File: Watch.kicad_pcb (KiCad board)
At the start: 2 copper layers, 34.5 x 38.6 mm, 42 parts, among them J1 USB_C_Receptacle_USB2.0_14P, Q1 2N3904, Q2 2N3904, Q3 2N3904, Q4 2N3904, SW1 SW_Push, SW3 SW_Push, SW4 SW_Push, U1 MCP73831-2-OT, U3 AP2112K-3.3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

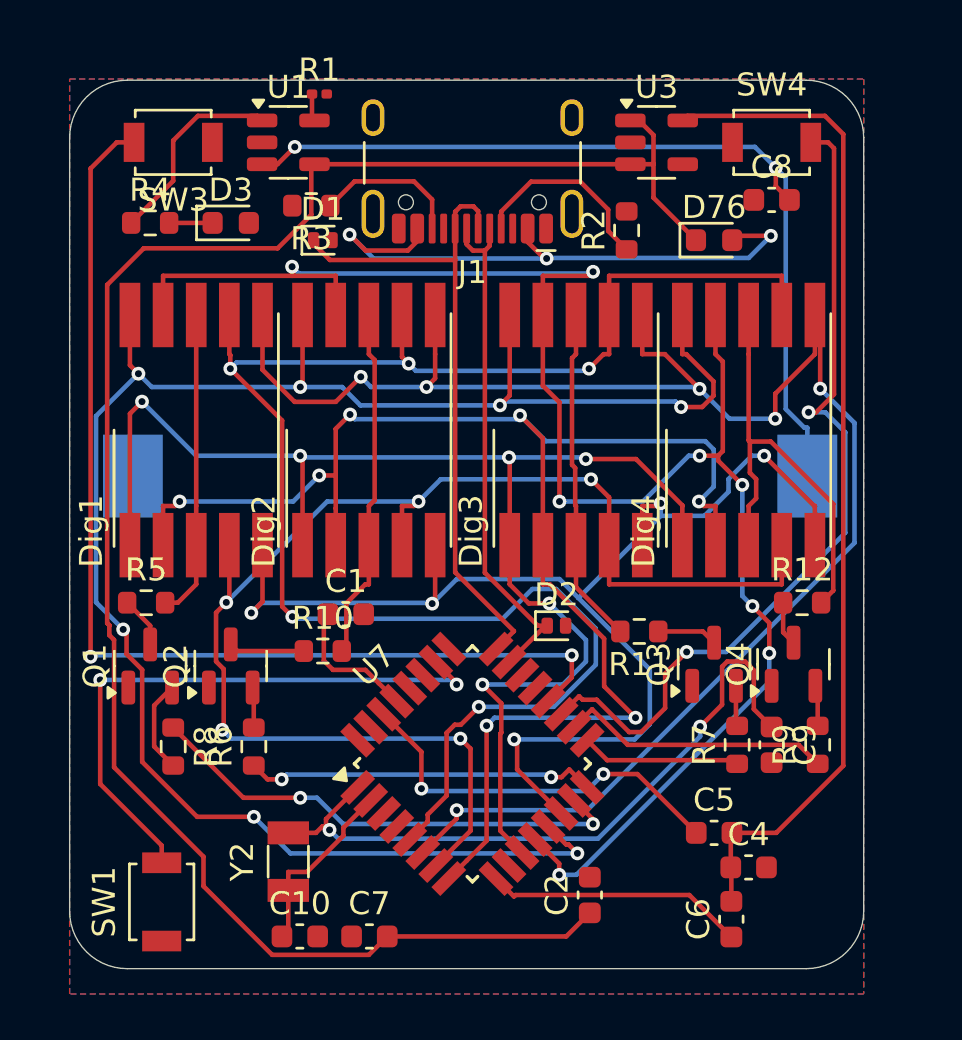
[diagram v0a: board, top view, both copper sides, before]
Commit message: Add blender, session 4, new render
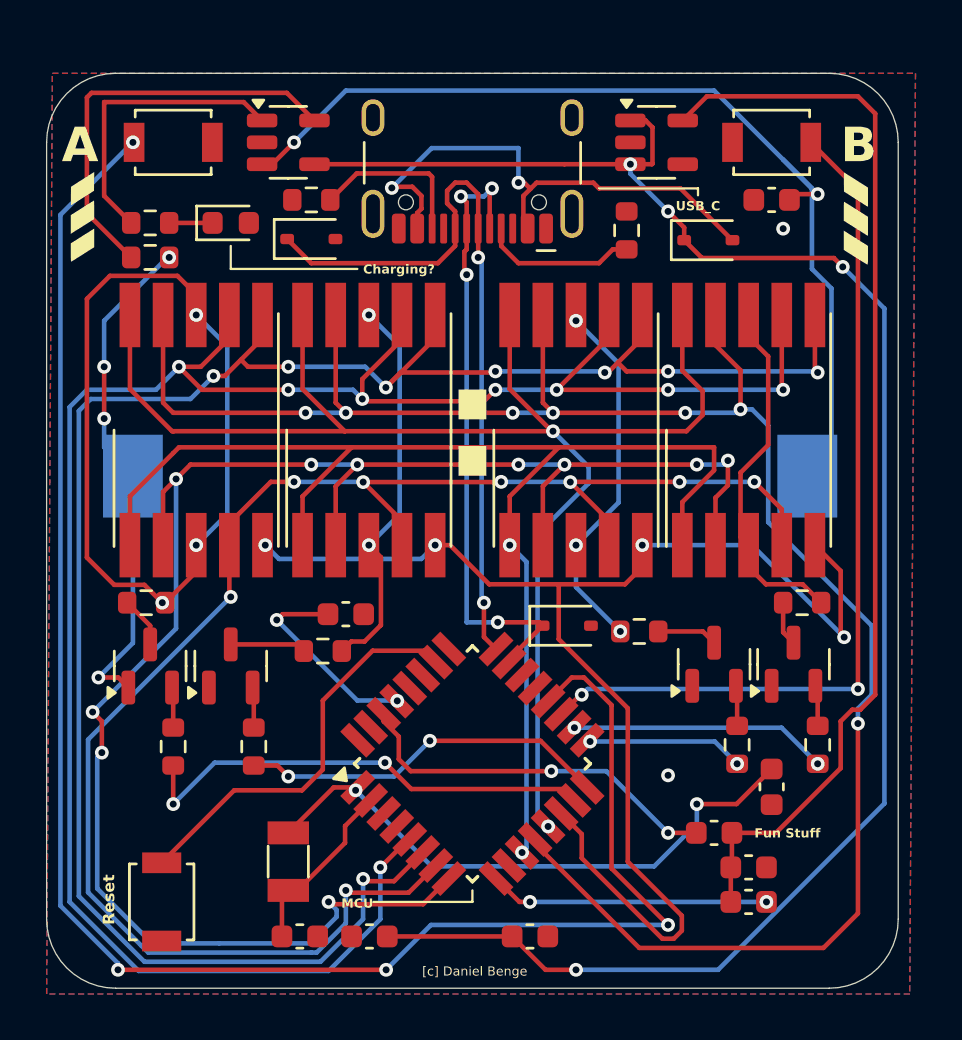
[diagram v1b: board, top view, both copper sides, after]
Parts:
- added G1: LOGO, LOGO, F.Cu at (160.6, 86.2)
- added graphic2: LOGO, LOGO, F.Cu at (194.2, 86.3)
- D1, D2: footprint Diode_SMD:D_SOD-882D -> Diode_SMD:D_SOD-323
- D76: footprint Diode_SMD:D_0603_1608Metric -> Diode_SMD:D_SOD-323
- R1: footprint Resistor_SMD:R_0201_0603Metric -> Resistor_SMD:R_0603_1608Metric
- moved R1 10.2 mm to (163.5, 88.0)
- moved C2 3.16 mm to (180.0, 117.5), turned to 0 degrees
- moved C9 1.83 mm to (190.5, 111.0)
- moved C6 1.06 mm to (189.5, 116.0), turned to 180 degrees
- moved D1 0.50 mm to (170.5, 87.2)
- moved D2 0.45 mm to (181.6, 104.0)
- moved D76 0.25 mm to (187.8, 87.2)
- moved R3 0.25 mm to (170.5, 85.5)
- turned R8 to 90 degrees
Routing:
- net Btn2: track 46.9 -> 77.3 mm, vias 2 -> 4
- net Net-(Dig1-CA-Pad3): track 13.4 -> 35.9 mm, vias 0 -> 3
- net GND: track 0.00 -> 22.1 mm, vias 0 -> 6
- net Net-(U1-PROG): track 1.19 -> 18.2 mm
- net G: track 80.8 -> 65.4 mm, vias 7 -> 2
- net A: track 75.1 -> 89.3 mm, vias 5 -> 8
- net B: track 73.8 -> 86.1 mm, vias 6 -> 8
- net C: track 59.9 -> 71.0 mm, vias 5 -> 8
- net D: track 66.6 -> 77.0 mm, vias 7 -> 10
- net Net-(U7-~{RESET}): track 26.0 -> 17.7 mm, vias 2 -> 0
- net F: track 76.3 -> 84.1 mm, vias 8 -> 7
- net Net-(BT1-+): track 38.7 -> 43.7 mm
- net D-: track 22.6 -> 27.5 mm, vias 0 -> 4
- net A0: track 30.2 -> 25.5 mm
- net Net-(U1-STAT): track 8.73 -> 12.9 mm
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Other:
- board size 34.5 x 38.6 mm -> 37 x 39.8 mm
- board text added: ":"
- board text added: "A"
- board text added: "B"
- board text added: "Charging?"
- board text added: "Fun Stuff"
- board text added: "JLCJLCJLCJLC"
- board text added: "MCU"
- board text added: "Reset"
- board text added: "USB_C"
- board text added: "[c] Daniel Benge"

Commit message: Fix PCB by adding test points
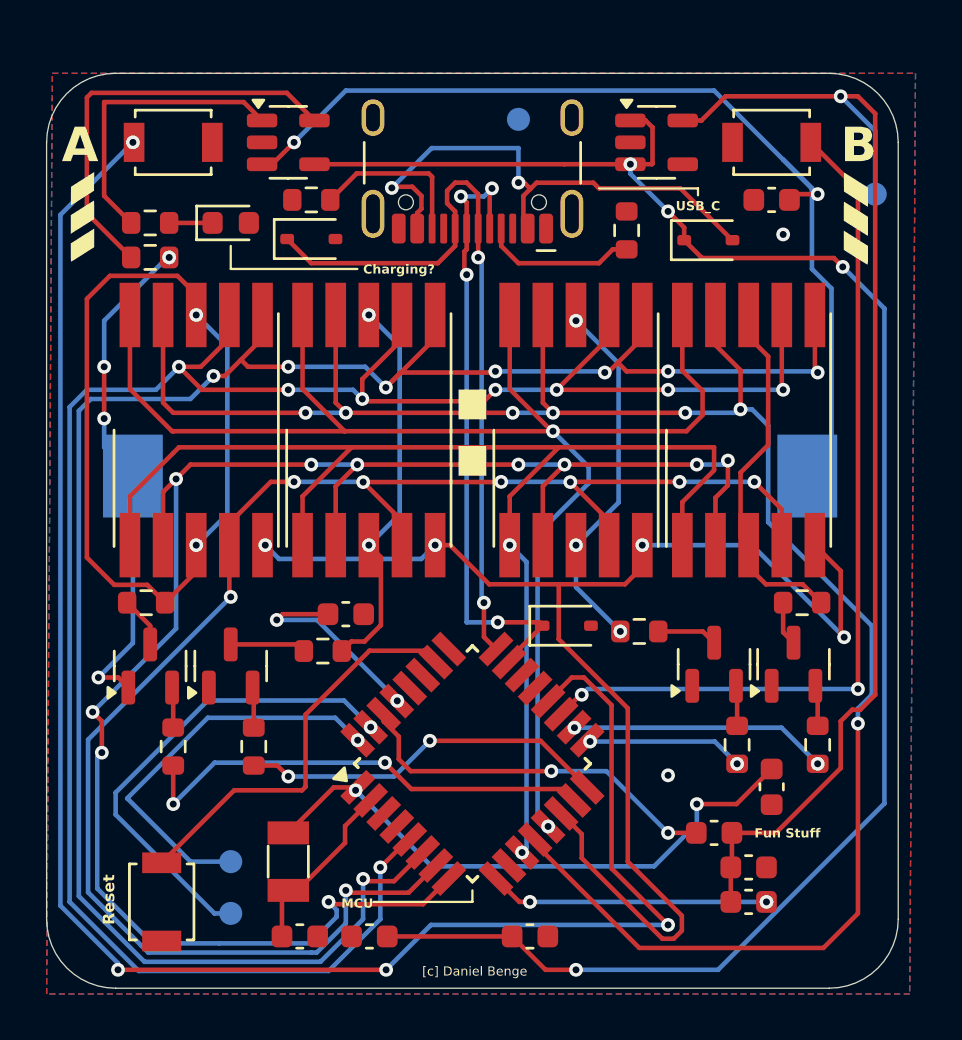
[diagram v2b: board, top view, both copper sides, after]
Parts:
- added 3.3V: TestPoint, TestPoint:TestPoint_Pad_D1.0mm, B.Cu at (195.0, 85.2)
- added GND: TestPoint, TestPoint:TestPoint_Pad_D1.0mm, B.Cu at (179.5, 82.0)
- added SWDIO: TestPoint, TestPoint:TestPoint_Pad_D1.0mm, B.Cu at (167.0, 114.2)
- added swdclck: TestPoint, TestPoint:TestPoint_Pad_D1.0mm, B.Cu at (167.0, 116.5)
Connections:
- net +3.3V renamed TP_3.3V
- U7 pad 31: unconnected-(U7-PA30-Pad31) -> TP_SWDCLK
- U7 pad 32: unconnected-(U7-PA31-Pad32) -> TP_SWDIO
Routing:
- net TP_SWDCLK: track 0.00 -> 21.0 mm, vias 0 -> 1
- net TP_SWDIO: track 0.00 -> 17.5 mm, vias 0 -> 1
- net TP_3.3V: track 47.3 -> 52.2 mm, vias 0 -> 1
- net Net-(Dig1-CA-Pad3): track 35.9 -> 36.0 mm, vias 3 -> 2

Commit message: Better test points
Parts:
- renumbered 3.3V to TP1, GND to TP2, SWDIO to TP3, swdclck to TP4
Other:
- board text added: "3.3V"
- board text added: "GND"
- board text added: "SWDCLCK"
- board text added: "SWDIO"

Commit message: Tiny improvements
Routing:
- net G: track 65.4 -> 64.4 mm
